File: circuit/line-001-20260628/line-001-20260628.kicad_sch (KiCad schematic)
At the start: 220 parts, among them J1 Conn_01x02_Pin, J2 Conn_01x02_Pin, J3 Conn_02x03_Odd_Even, J4 USB_C_Receptacle_USB2.0_16P, Q1 Q_Photo_NPN_CE, Q10 Q_Photo_NPN_CE, Q11 Q_Photo_NPN_CE, Q12 Q_Photo_NPN_CE, Q13 Q_Photo_NPN_CE, Q14 Q_Photo_NPN_CE, Q15 Q_Photo_NPN_CE, Q16 Q_Photo_NPN_CE, Q17 Q_Photo_NPN_CE, Q18 Q_Photo_NPN_CE, Q19 Q_Photo_NPN_CE, Q2 Q_Photo_NPN_CE, Q20 Q_Photo_NPN_CE, Q21 Q_Photo_NPN_CE, Q22 Q_Photo_NPN_CE, Q23 Q_Photo_NPN_CE, Q24 Q_Photo_NPN_CE, Q25 Q_Photo_NPN_CE, Q26 Q_Photo_NPN_CE, Q27 Q_Photo_NPN_CE, Q28 Q_Photo_NPN_CE, Q29 Q_Photo_NPN_CE, Q3 Q_Photo_NPN_CE, Q30 Q_Photo_NPN_CE, Q31 Q_Photo_NPN_CE, Q32 Q_Photo_NPN_CE, Q37 Q_Photo_NPN_CE, Q38 Q_Photo_NPN_CE, Q39 Q_Photo_NPN_CE, Q4 Q_Photo_NPN_CE, Q40 Q_Photo_NPN_CE, Q5 Q_Photo_NPN_CE, Q6 Q_Photo_NPN_CE, Q7 Q_Photo_NPN_CE, Q8 Q_Photo_NPN_CE, Q9 Q_Photo_NPN_CE, SW1 SW_Push, SW2 SW_SPDT, U1 LM393DR, U10 LM393DR, U11 LM393DR, U12 LM393DR, U13 LM393DR, U14 LM393DR, U15 LM393DR, U16 LM393DR, U17 ATmega2560-16A, U18 CH340G, U2 LM393DR, U3 LM393DR, U4 LM393DR, U5 LM393DR, U6 LM393DR, U7 LM393DR, U8 LM393DR, U9 LM393DR, Y1 16MHz, Y2 12MHz

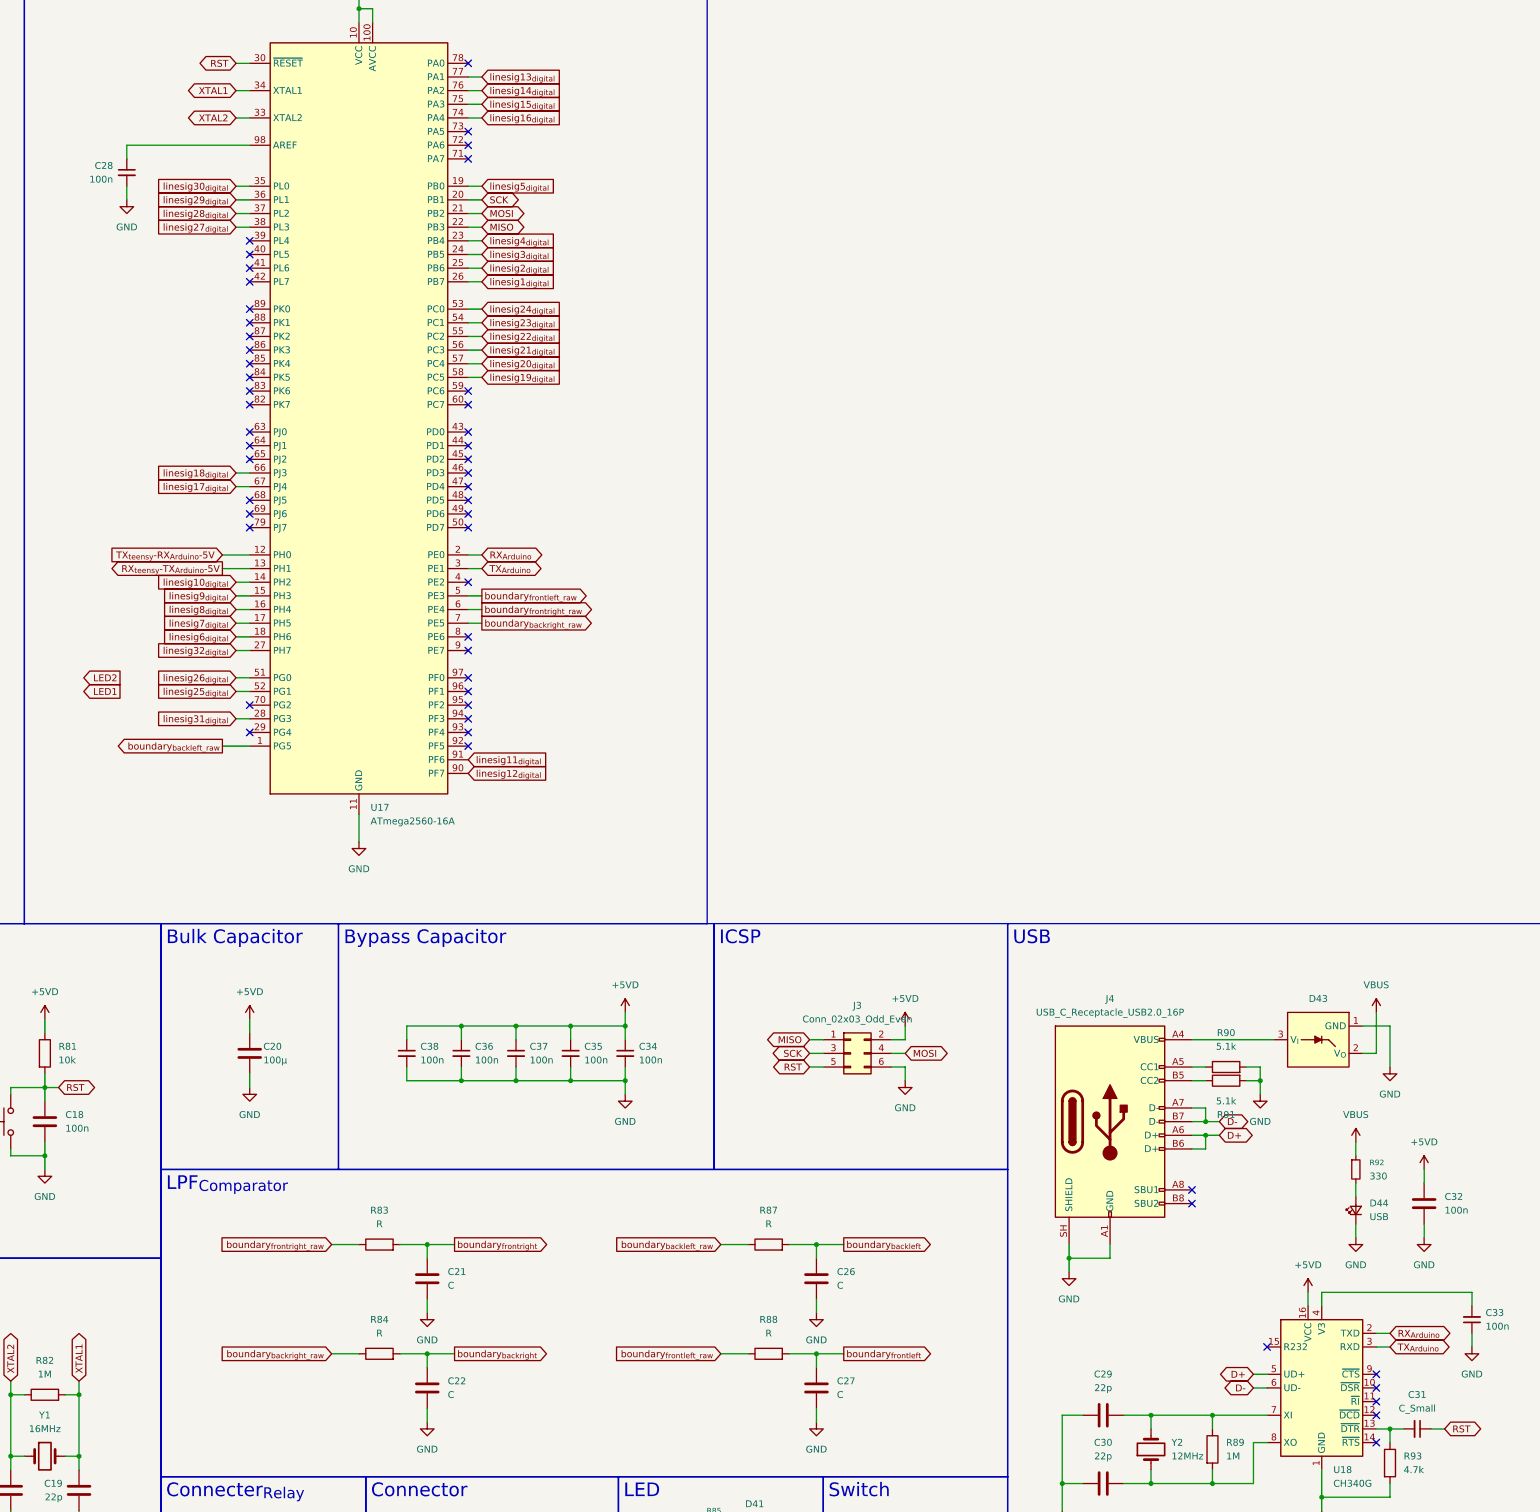
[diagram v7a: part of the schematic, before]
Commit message: Update ラインセンサ基板のシルクスクリーンを整えてLEDを取り付けた
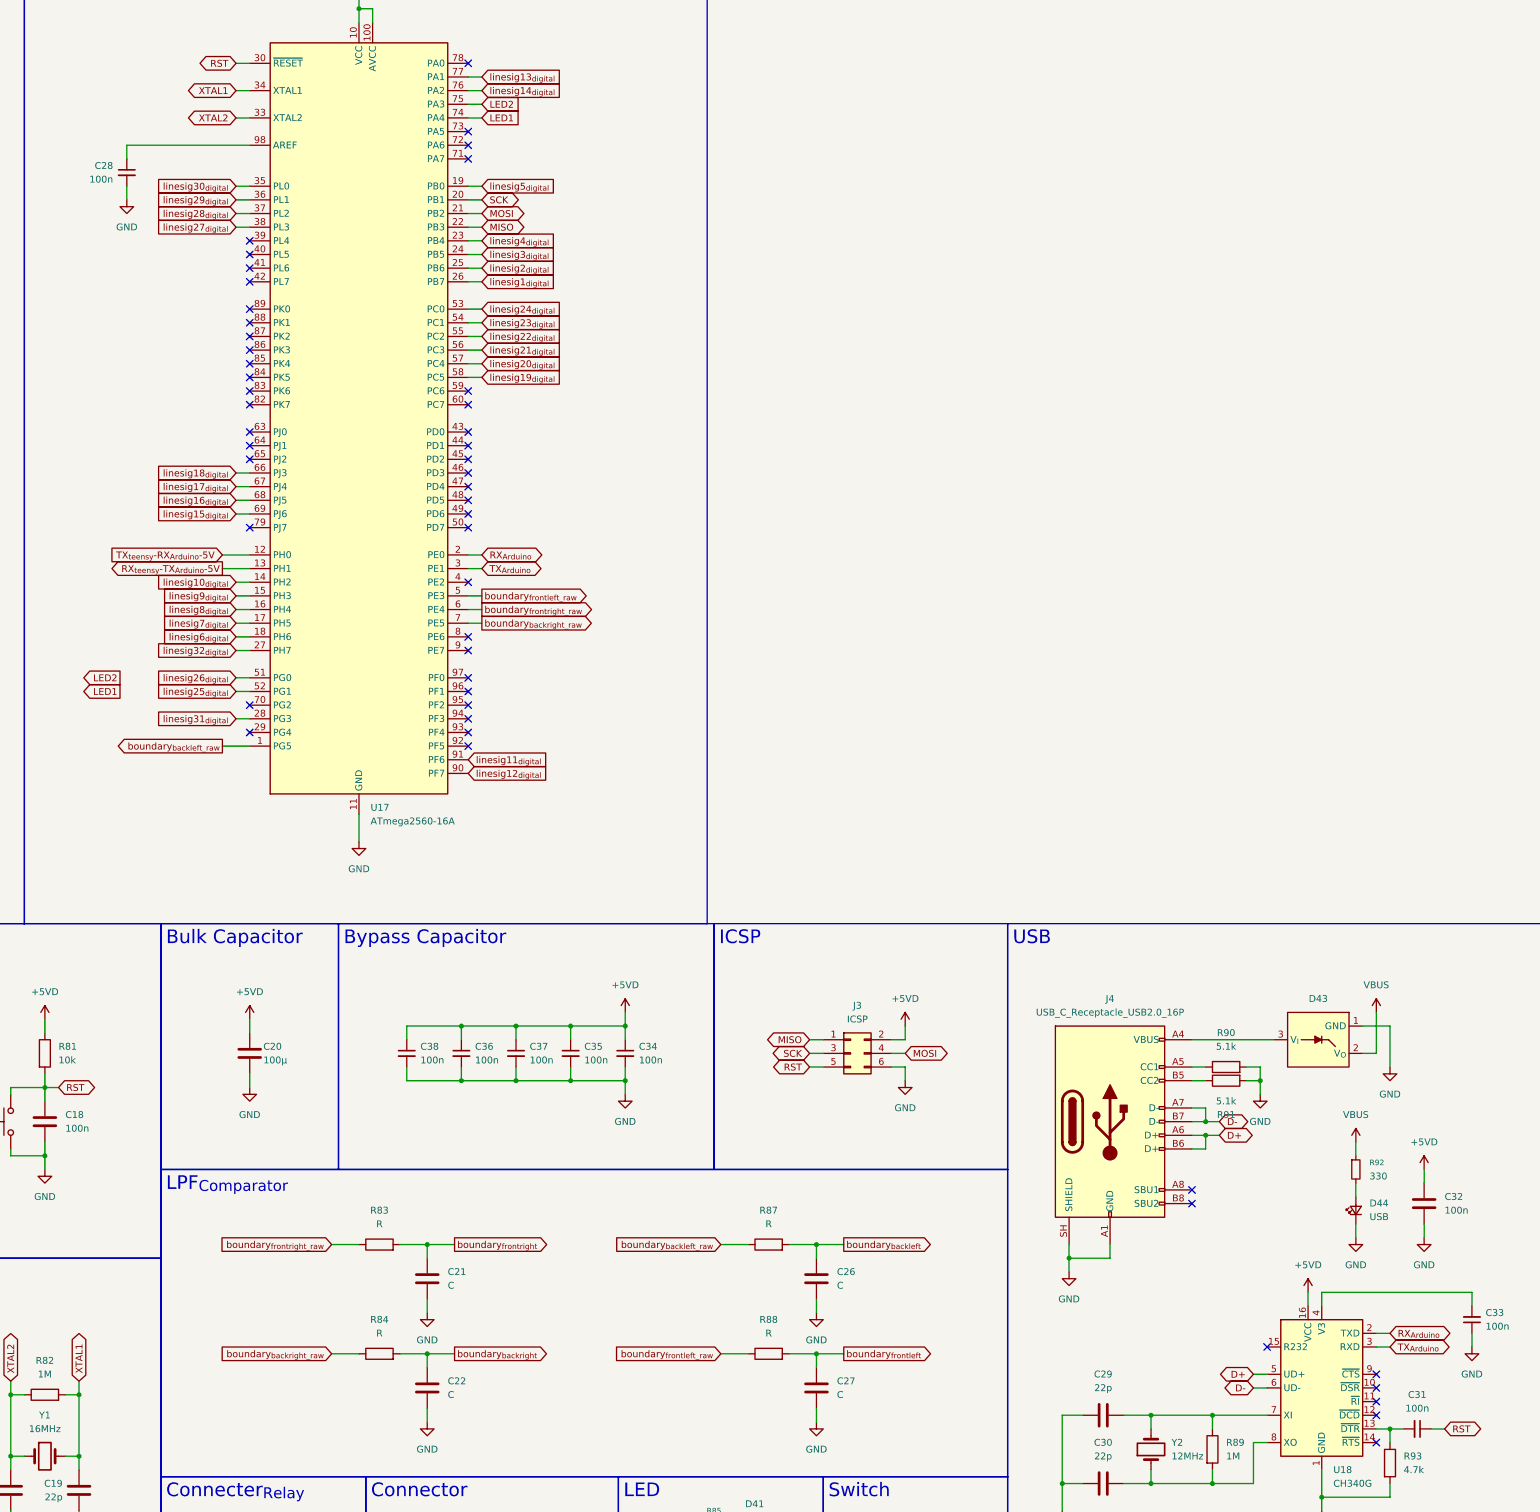
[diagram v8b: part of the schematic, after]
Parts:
- C31: value C_Small -> 100n
- J3: value Conn_02x03_Odd_Even -> ICSP
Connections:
- net LED1: now also U17.74 (PA4)
- net LED2: now also U17.75 (PA3)
- net linesig15_{digital}: now also U17.69 (PJ6); no longer U17.75 (PA3)
- net linesig16_{digital}: now also U17.68 (PJ5); no longer U17.74 (PA4)
- no-connect marks 51 -> 49
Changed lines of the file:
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@@
 	)
 	(no_connect
-		(at 321.31 123.19)
-	)
-	(no_connect
 		(at 361.95 41.91)
 	)
@@
 	)
 	(no_connect
-		(at 321.31 125.73)
-	)
-	(no_connect
 		(at 361.95 148.59)
 	)
@@
 	(wire
 		(pts
+			(xy 318.77 123.19) (xy 321.31 123.19)
+		)
+		(stroke
+			(width 0)
+			(type default)
+		)
+	)
+	(wire
+		(pts
 			(xy 95.25 306.07) (xy 97.79 306.07)
 		)
@@
 	(wire
 		(pts
+			(xy 318.77 125.73) (xy 321.31 125.73)
+		)
+		(stroke
+			(width 0)
+			(type default)
+		)
+	)
+	(wire
+		(pts
 			(xy 20.32 58.42) (xy 20.32 72.39)
 		)
@@
 		)
 	)
+	(global_label "LED2"
+		(shape input)
+		(at 364.49 49.53 0)
+		(fields_autoplaced yes)
+		(effects
+			(font
+				(size 1.27 1.27)
+			)
+			(justify left)
+		)
+		(property "Intersheetrefs" "${INTERSHEET_REFS}"
+			(at 372.2877 49.53 0)
+			(hide yes)
+			(show_name no)
+			(do_not_autoplace no)
+			(effects
+				(font
+					(size 1.27 1.27)
+				)
+				(justify left)
+			)
+		)
+	)
 	(global_label "linesig23_{digital}"
 		(shape output)
@@
 		)
 	)
+	(global_label "LED1"
+		(shape input)
+		(at 364.49 52.07 0)
+		(fields_autoplaced yes)
+		(effects
+			(font
+				(size 1.27 1.27)
+			)
+			(justify left)
+		)
+		(property "Intersheetrefs" "${INTERSHEET_REFS}"
+			(at 372.2877 52.07 0)
+			(hide yes)
+			(show_name no)
+			(do_not_autoplace no)
+			(effects
+				(font
+					(size 1.27 1.27)
+				)
+				(justify left)
+			)
+		)
+	)
 	(global_label "linesig25_{raw}"
 		(shape output)
@@
 	(global_label "linesig16_{digital}"
 		(shape input)
-		(at 364.49 52.07 0)
+		(at 318.77 123.19 180)
 		(fields_autoplaced yes)
 		(effects
@@
 				(size 1.27 1.27)
 			)
-			(justify left)
+			(justify right)
 		)
 		(property "Intersheetrefs" "${INTERSHEET_REFS}"
-			(at 377.2321 52.07 0)
+			(at 306.0279 123.19 0)
 			(hide yes)
 			(show_name no)
@@
 					(size 1.27 1.27)
 				)
-				(justify left)
+				(justify right)
 			)
 		)
@@
 	(global_label "linesig15_{digital}"
 		(shape input)
-		(at 364.49 49.53 0)
+		(at 318.77 125.73 180)
 		(fields_autoplaced yes)
 		(effects
@@
 				(size 1.27 1.27)
 			)
-			(justify left)
+			(justify right)
 		)
 		(property "Intersheetrefs" "${INTERSHEET_REFS}"
-			(at 377.2321 49.53 0)
+			(at 306.0279 125.73 0)
 			(hide yes)
 			(show_name no)
@@
 					(size 1.27 1.27)
 				)
-				(justify left)
+				(justify right)
 			)
 		)
@@
 			)
 		)
-		(property "Value" "Conn_02x03_Odd_Even"
+		(property "Value" "ICSP"
 			(at 434.34 219.71 0)
 			(show_name no)
@@
 			)
 		)
-		(property "Value" "C_Small"
+		(property "Value" "100n"
 			(at 538.4736 292.1 90)
 			(show_name no)
